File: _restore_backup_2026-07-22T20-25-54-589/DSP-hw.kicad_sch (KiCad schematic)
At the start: 50 parts, among them Q1 BC327, Q2 AO3400A, SW1 SW_Push, SW8 SW_Push, U1 ADAU1701, U2 CAT24C256, U3 AMS1117-3.3, Y1 12.228M

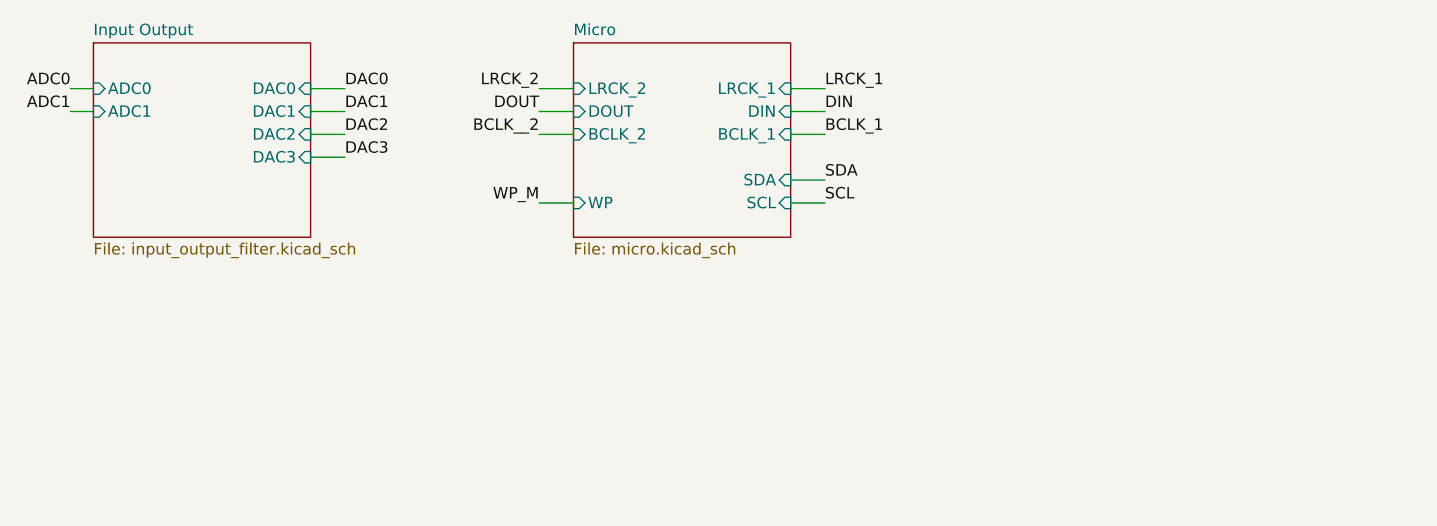
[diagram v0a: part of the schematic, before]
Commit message: aggiunto cad 3d dei connettori
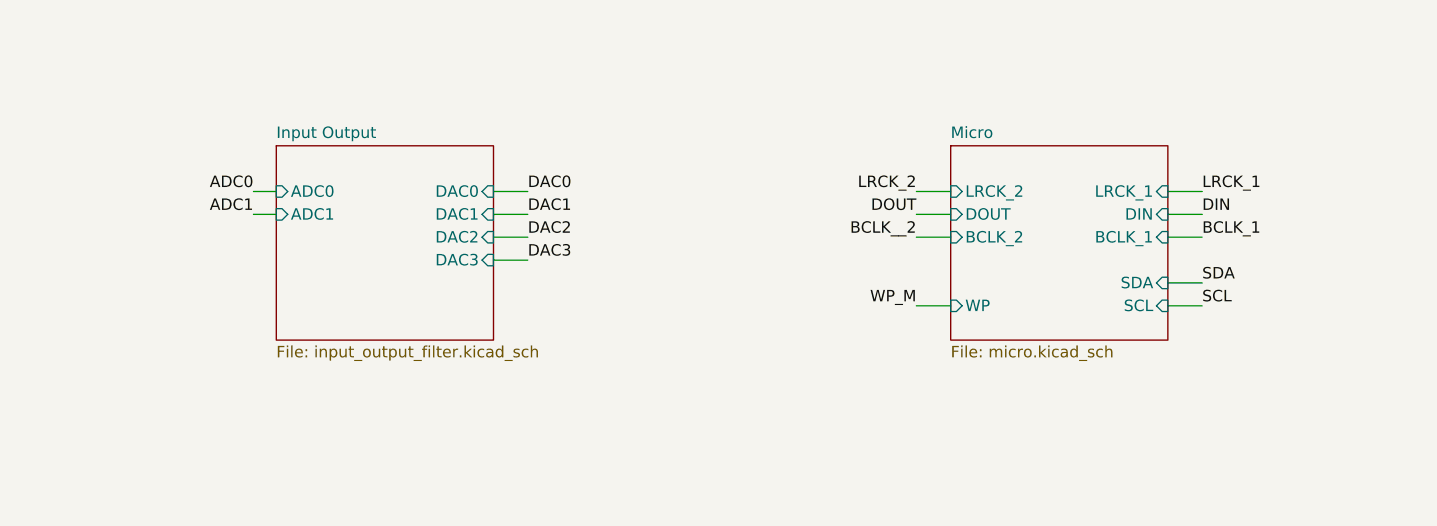
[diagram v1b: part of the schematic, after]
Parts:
- RV1, RV2: footprint Potentiometer_THT:Potentiometer_Alps_RK09Y11_Single_Horizontal -> Potentiometer_THT:Potentiometer_Alps_RK097_Single_Horizontal
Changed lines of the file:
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@@
 	(wire
 		(pts
-			(xy 48.26 33.02) (xy 52.07 33.02)
+			(xy 68.58 44.45) (xy 72.39 44.45)
 		)
 		(stroke
@@
 	(wire
 		(pts
-			(xy 73.66 25.4) (xy 77.47 25.4)
+			(xy 115.57 36.83) (xy 119.38 36.83)
 		)
 		(stroke
@@
 	(wire
 		(pts
-			(xy 101.6 27.94) (xy 105.41 27.94)
+			(xy 143.51 39.37) (xy 147.32 39.37)
 		)
 		(stroke
@@
 	(wire
 		(pts
-			(xy 48.26 27.94) (xy 52.07 27.94)
+			(xy 68.58 39.37) (xy 72.39 39.37)
 		)
 		(stroke
@@
 	(wire
 		(pts
-			(xy 101.6 35.56) (xy 105.41 35.56)
+			(xy 143.51 46.99) (xy 147.32 46.99)
 		)
 		(stroke
@@
 	(wire
 		(pts
-			(xy 21.59 27.94) (xy 24.13 27.94)
+			(xy 41.91 39.37) (xy 44.45 39.37)
 		)
 		(stroke
@@
 	(wire
 		(pts
-			(xy 48.26 25.4) (xy 52.07 25.4)
+			(xy 68.58 36.83) (xy 72.39 36.83)
 		)
 		(stroke
@@
 	(wire
 		(pts
-			(xy 73.66 30.48) (xy 77.47 30.48)
+			(xy 115.57 41.91) (xy 119.38 41.91)
 		)
 		(stroke
@@
 	(wire
 		(pts
-			(xy 101.6 38.1) (xy 105.41 38.1)
+			(xy 143.51 49.53) (xy 147.32 49.53)
 		)
 		(stroke
@@
 	(wire
 		(pts
-			(xy 21.59 25.4) (xy 24.13 25.4)
+			(xy 41.91 36.83) (xy 44.45 36.83)
 		)
 		(stroke
@@
 	(wire
 		(pts
-			(xy 73.66 38.1) (xy 77.47 38.1)
+			(xy 115.57 49.53) (xy 119.38 49.53)
 		)
 		(stroke
@@
 	(wire
 		(pts
-			(xy 101.6 30.48) (xy 105.41 30.48)
+			(xy 143.51 41.91) (xy 147.32 41.91)
 		)
 		(stroke
@@
 	(wire
 		(pts
-			(xy 73.66 27.94) (xy 77.47 27.94)
+			(xy 115.57 39.37) (xy 119.38 39.37)
 		)
 		(stroke
@@
 	(wire
 		(pts
-			(xy 48.26 30.48) (xy 52.07 30.48)
+			(xy 68.58 41.91) (xy 72.39 41.91)
 		)
 		(stroke
@@
 	(wire
 		(pts
-			(xy 101.6 25.4) (xy 105.41 25.4)
+			(xy 143.51 36.83) (xy 147.32 36.83)
 		)
 		(stroke
@@
 	)
 	(label "DIN"
-		(at 105.41 27.94 0)
+		(at 147.32 39.37 0)
 		(effects
 			(font
@@
 	)
 	(label "ADC1"
-		(at 21.59 27.94 180)
+		(at 41.91 39.37 180)
 		(effects
 			(font
@@
 	)
 	(label "DAC3"
-		(at 52.07 33.02 0)
+		(at 72.39 44.45 0)
 		(effects
 			(font
@@
 	)
 	(label "WP_M"
-		(at 73.66 38.1 180)
+		(at 115.57 49.53 180)
 		(effects
 			(font
@@
 	)
 	(label "ADC0"
-		(at 21.59 25.4 180)
+		(at 41.91 36.83 180)
 		(effects
 			(font
@@
 	)
 	(label "DAC1"
-		(at 52.07 27.94 0)
+		(at 72.39 39.37 0)
 		(effects
 			(font
@@
 	)
 	(label "LRCK_2"
-		(at 73.66 25.4 180)
+		(at 115.57 36.83 180)
 		(effects
 			(font
@@
 	)
 	(label "BCLK_1"
-		(at 105.41 30.48 0)
+		(at 147.32 41.91 0)
 		(effects
 			(font
@@
 	)
 	(label "LRCK_1"
-		(at 105.41 25.4 0)
+		(at 147.32 36.83 0)
 		(effects
 			(font
@@
 	)
 	(label "SCL"
-		(at 105.41 38.1 0)
+		(at 147.32 49.53 0)
 		(effects
 			(font
@@
 	)
 	(label "DAC0"
-		(at 52.07 25.4 0)
+		(at 72.39 36.83 0)
 		(effects
 			(font
@@
 	)
 	(label "SDA"
-		(at 105.41 35.56 0)
+		(at 147.32 46.99 0)
 		(effects
 			(font
@@
 	)
 	(label "DAC2"
-		(at 52.07 30.48 0)
+		(at 72.39 41.91 0)
 		(effects
 			(font
@@
 	)
 	(label "DOUT"
-		(at 73.66 27.94 180)
+		(at 115.57 39.37 180)
 		(effects
 			(font
@@
 	)
 	(label "BCLK__2"
-		(at 73.66 30.48 180)
+		(at 115.57 41.91 180)
 		(effects
 			(font
@@
 			)
 		)
-		(property "Footprint" "Potentiometer_THT:Potentiometer_Alps_RK09Y11_Single_Horizontal"
+		(property "Footprint" "Potentiometer_THT:Potentiometer_Alps_RK097_Single_Horizontal"
 			(at 105.41 135.89 0)
 			(hide yes)
@@
 			)
 		)
-		(property "Footprint" "Potentiometer_THT:Potentiometer_Alps_RK09Y11_Single_Horizontal"
+		(property "Footprint" "Potentiometer_THT:Potentiometer_Alps_RK097_Single_Horizontal"
 			(at 124.46 135.89 0)
 			(hide yes)
@@
 	)
 	(sheet
-		(at 77.47 20.32)
+		(at 119.38 31.75)
 		(size 24.13 21.59)
 		(exclude_from_sim no)
@@
 		)
 		(property "Sheetname" "Micro"
-			(at 77.47 19.6084 0)
+			(at 119.38 31.0384 0)
 			(show_name no)
 			(do_not_autoplace no)
@@
 		)
 		(property "Sheetfile" "micro.kicad_sch"
-			(at 77.47 42.4946 0)
+			(at 119.38 53.9246 0)
 			(show_name no)
 			(do_not_autoplace no)
@@
 		)
 		(pin "SCL" input
-			(at 101.6 38.1 0)
+			(at 143.51 49.53 0)
 			(effects
 				(font
@@
 		)
 		(pin "SDA" input
-			(at 101.6 35.56 0)
+			(at 143.51 46.99 0)
 			(effects
 				(font
@@
 		)
 		(pin "BCLK_1" input
-			(at 101.6 30.48 0)
+			(at 143.51 41.91 0)
 			(effects
 				(font
@@
 		)
 		(pin "BCLK_2" input
-			(at 77.47 30.48 180)
+			(at 119.38 41.91 180)
 			(effects
 				(font
@@
 		)
 		(pin "DIN" input
-			(at 101.6 27.94 0)
+			(at 143.51 39.37 0)
 			(effects
 				(font
@@
 		)
 		(pin "DOUT" input
-			(at 77.47 27.94 180)
+			(at 119.38 39.37 180)
 			(effects
 				(font
@@
 		)
 		(pin "LRCK_1" input
-			(at 101.6 25.4 0)
+			(at 143.51 36.83 0)
 			(effects
 				(font
@@
 		)
 		(pin "LRCK_2" input
-			(at 77.47 25.4 180)
+			(at 119.38 36.83 180)
 			(effects
 				(font
@@
 		)
 		(pin "WP" input
-			(at 77.47 38.1 180)
+			(at 119.38 49.53 180)
 			(effects
 				(font
@@
 	)
 	(sheet
-		(at 24.13 20.32)
+		(at 44.45 31.75)
 		(size 24.13 21.59)
 		(exclude_from_sim no)
@@
 		)
 		(property "Sheetname" "Input Output"
-			(at 24.13 19.6084 0)
+			(at 44.45 31.0384 0)
 			(show_name no)
 			(do_not_autoplace no)
@@
 		)
 		(property "Sheetfile" "input_output_filter.kicad_sch"
-			(at 24.13 42.4946 0)
+			(at 44.45 53.9246 0)
 			(show_name no)
 			(do_not_autoplace no)
@@
 		)
 		(pin "ADC0" input
-			(at 24.13 25.4 180)
+			(at 44.45 36.83 180)
 			(effects
 				(font
@@
 		)
 		(pin "ADC1" input
-			(at 24.13 27.94 180)
+			(at 44.45 39.37 180)
 			(effects
 				(font
@@
 		)
 		(pin "DAC0" input
-			(at 48.26 25.4 0)
+			(at 68.58 36.83 0)
 			(effects
 				(font
@@
 		)
 		(pin "DAC1" input
-			(at 48.26 27.94 0)
+			(at 68.58 39.37 0)
 			(effects
 				(font
@@
 		)
 		(pin "DAC2" input
-			(at 48.26 30.48 0)
+			(at 68.58 41.91 0)
 			(effects
 				(font
@@
 		)
 		(pin "DAC3" input
-			(at 48.26 33.02 0)
+			(at 68.58 44.45 0)
 			(effects
 				(font
